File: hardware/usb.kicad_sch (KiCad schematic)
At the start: 4 parts, among them J21 USB_C_Receptacle_USB2.0_16P

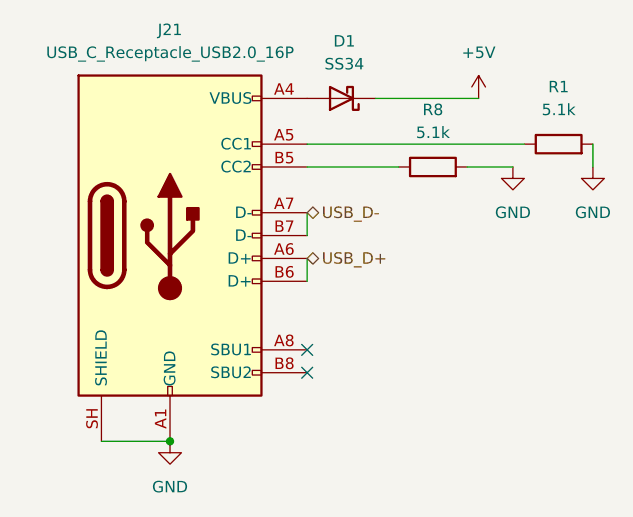
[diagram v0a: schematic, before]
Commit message: place the stuff on the pcb
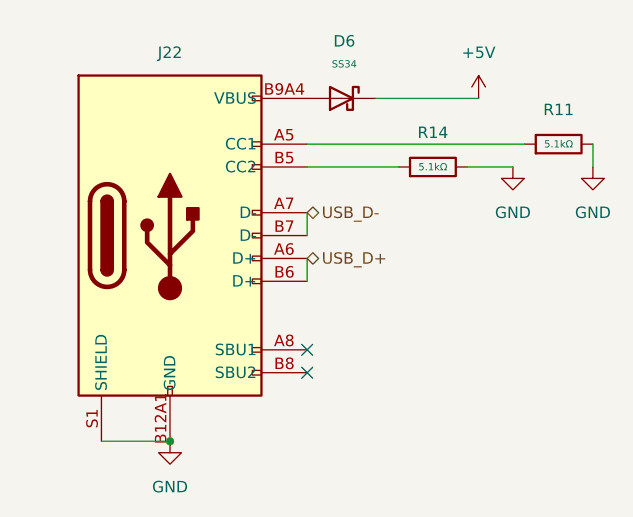
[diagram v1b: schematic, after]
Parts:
- removed D1: SS34, Diode_SMD:D_SMA, symbol Device:D_Schottky
- removed J21: USB_C_Receptacle_USB2.0_16P, symbol Connector:USB_C_Receptacle_USB2.0_16P
- removed R1, R8: 5.1k, symbol Device:R
- added D6: SS34, PCM_JLCPCB:D_SMA, symbol PCM_JLCPCB-Diodes:Schottky,SS34
- added J22: Connector, USB-TYPE-C-16P, PCM_JLCPCB:TYPE-C-SMD_HX-TYPE-C-16PIN, symbol PCM_JLCPCB-Extended:Connector, USB-TYPE-C-16P
- added R11, R14: 5.1kΩ, PCM_JLCPCB:R_0603, symbol PCM_JLCPCB-Resistors:0603,5.1kΩ
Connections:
- net +5V: now also D6.1
- net GND: now also J22.A12B1 (GND), J22.B12A1 (GND), J22.S1 (SHIELD), R11.2, R14.2
- net USB_D+: now also J22.A6 (D+), J22.B6 (D+)
- net USB_D-: now also J22.A7 (D-), J22.B7 (D-)
- new net: J22.B5 (CC2), R14.1
- new net: J22.A5 (CC1), R11.1
- new net: D6.2, J22.A9B4 (VBUS), J22.B9A4 (VBUS)
